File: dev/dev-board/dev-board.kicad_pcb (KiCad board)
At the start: 2 copper layers, 95 x 95 mm, 108 parts, among them J1 Conn_01x04_Pin, J2 Conn_01x14_Socket, P1 HDR-IDC-2.54-2X5P, Q1 BSS138, Q2 BSS138, Q3 BSS138, Q4 BSS138, SW1 TS342A2P, SW2 TS342A2P, SW3 TS342A2P, SW4 TS342A2P, SW6 TSC015A03526A, SW7 TSC015A03526A, SW8 TSC015A03526A, SW9 TSC015A03526A, U1 ESP32-WROVER-IE(16MB), U10 TPS2065CDBV, U11 PESD5V0U2BT, U12 PESD5V0S1BA_C5261083, U13 PCM5102APWR, U2 ESP32-S3-WROOM-1(N16R8), U3 CP2105-F01-GMR, U4 TPS2065CDBV, U5 AP7361C-33E, U6 PESD5V0U2BT, U7 PESD5V0S1BA_C5261083, U8 ZX-HY2.0-4PWZ, U9 ZX-HY2.0-4PWZ

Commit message: making CAD
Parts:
- moved R34 31.1 mm to (-100.0, 6.00), turned to 180 degrees
- moved R31 29.3 mm to (-93.3, 13.5), turned to 180 degrees
- moved R32 26.4 mm to (-93.3, 11.8), turned to 180 degrees
- moved C24 25.0 mm to (-94.5, 24.8)
- moved R30 21.4 mm to (-93.3, 15.3), turned to 180 degrees
- moved C31 18.6 mm to (-110.7, 16.2), turned to -90 degrees
- moved C22 17.8 mm to (-101.2, 19.0), turned to 90 degrees
- moved C32 15.5 mm to (-117.5, 17.8), turned to 180 degrees
- moved R29 14.9 mm to (-114.2, 17.8)
- moved C30 13.4 mm to (-105.8, 12.2), turned to 90 degrees
- moved C23 8.85 mm to (-99.5, 19.0), turned to 90 degrees
- moved LDO1 8.34 mm to (-96.5, 21.0)
- moved C29 7.86 mm to (-100.0, 8.77), turned to 180 degrees
- moved C25 7.74 mm to (-94.2, 9.00), turned to 90 degrees
- moved C28 7.71 mm to (-97.2, 8.00), turned to -90 degrees
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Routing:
- net /S3-ButtonUp: track 0.00 -> 127.9 mm, vias 0 -> 4
- net /S3-ButtonDown: track 0.00 -> 98.5 mm, vias 0 -> 6
- net /S3-ButtonCancel: track 0.00 -> 92.9 mm, vias 0 -> 6
- net /S3-ButtonEnter: track 0.00 -> 91.0 mm, vias 0 -> 8
- net +3V3: track 306.4 -> 375.0 mm, vias 13 -> 15
- net /VSPI-MOSI: track 0.00 -> 65.4 mm, vias 0 -> 3
- net /VSPI-TFT-RESET: track 0.00 -> 60.5 mm, vias 0 -> 1
- net /VSPI-SCLK: track 0.00 -> 59.2 mm, vias 0 -> 1
- net /VSPI-DC: track 0.00 -> 57.2 mm, vias 0 -> 5
- net /VSPI-CS: track 0.00 -> 55.1 mm, vias 0 -> 1
- net /VSPI-MISO: track 0.00 -> 53.6 mm, vias 0 -> 3
- net /S3-IO0: track 38.0 -> 74.1 mm, vias 2 -> 4
- net /WR-IO35: track 0.00 -> 27.3 mm
- net /WR-IO34: track 0.00 -> 25.6 mm
- net /WR-I2S-BLK: track 0.00 -> 25.0 mm
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
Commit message: making CAD
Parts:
- added REF**: MountingHole_3.2mm_M3, MountingHole:MountingHole_3.2mm_M3, F.Cu at (-120.0, 40.2)
- added REF**: MountingHole_3.2mm_M3, MountingHole:MountingHole_3.2mm_M3, F.Cu at (-120.2, -45.5)
- added REF**: MountingHole_3.2mm_M3, MountingHole:MountingHole_3.2mm_M3, F.Cu at (-34.5, 40.8)
- added REF**: MountingHole_3.2mm_M3, MountingHole:MountingHole_3.2mm_M3, F.Cu at (-34.2, -45.5)
- moved C17 5.80 mm to (-112.8, 37.8)
- moved C9 4.45 mm to (-41.0, 27.8)
- moved P1 4.12 mm to (-34.5, 30.2)
- moved LED1 2.25 mm to (-112.5, 41.0)
- moved C1 1.88 mm to (-45.2, -20.8)
- moved SW6 1.75 mm to (-120.8, -28.2)
- moved SW7 1.75 mm to (-113.0, -37.5)
- moved SW8 1.75 mm to (-120.8, -37.2)
- moved SW9 1.75 mm to (-113.0, -28.2)
- moved C2 0.96 mm to (-47.2, -18.2)
- moved U7 0.90 mm to (-42.2, -21.8), turned to 0 degrees
- moved U4 0.41 mm to (-42.2, -18.5)
- renumbered SW1 to SW1(S3-IO0), SW2 to SW2(WR-IO0), SW3 to SW3(S3-EN), SW4 to SW4(WR-EN)
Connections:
- net /CC1 renamed CC1
- net /CC2 renamed CC2
- net /D+ renamed D+
- net /D- renamed D-
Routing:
- net CC1: track 0.00 -> 32.9 mm, vias 0 -> 2
- net +3V3: track 375.0 -> 406.4 mm, vias 15 -> 17
- net VBUS: track 16.3 -> 46.9 mm, vias 0 -> 1
- net GND: track 0.00 -> 11.2 mm, vias 0 -> 498
- net D+: track 7.16 -> 16.7 mm, vias 0 -> 3
- net /S3-RMT: track 125.2 -> 115.9 mm
- net CC2: track 0.00 -> 8.19 mm
- net /S3-MTDO: track 26.0 -> 30.6 mm
- net /S3-USB-PWSW: track 84.5 -> 80.2 mm
- net /S3-MTCK: track 26.9 -> 23.7 mm
- net /S3-MTMS: track 30.3 -> 27.8 mm
- net /S3-MTDI: track 36.0 -> 33.6 mm
- net /S3-ButtonCancel: track 92.9 -> 95.0 mm, vias 6 -> 4
- net D-: track 11.7 -> 13.3 mm
- net VSYS: track 161.4 -> 159.9 mm
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- added copper zone on B.Cu, net GND
- added copper zone on F.Cu, net GND
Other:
- outline, holes or cut-outs redrawn

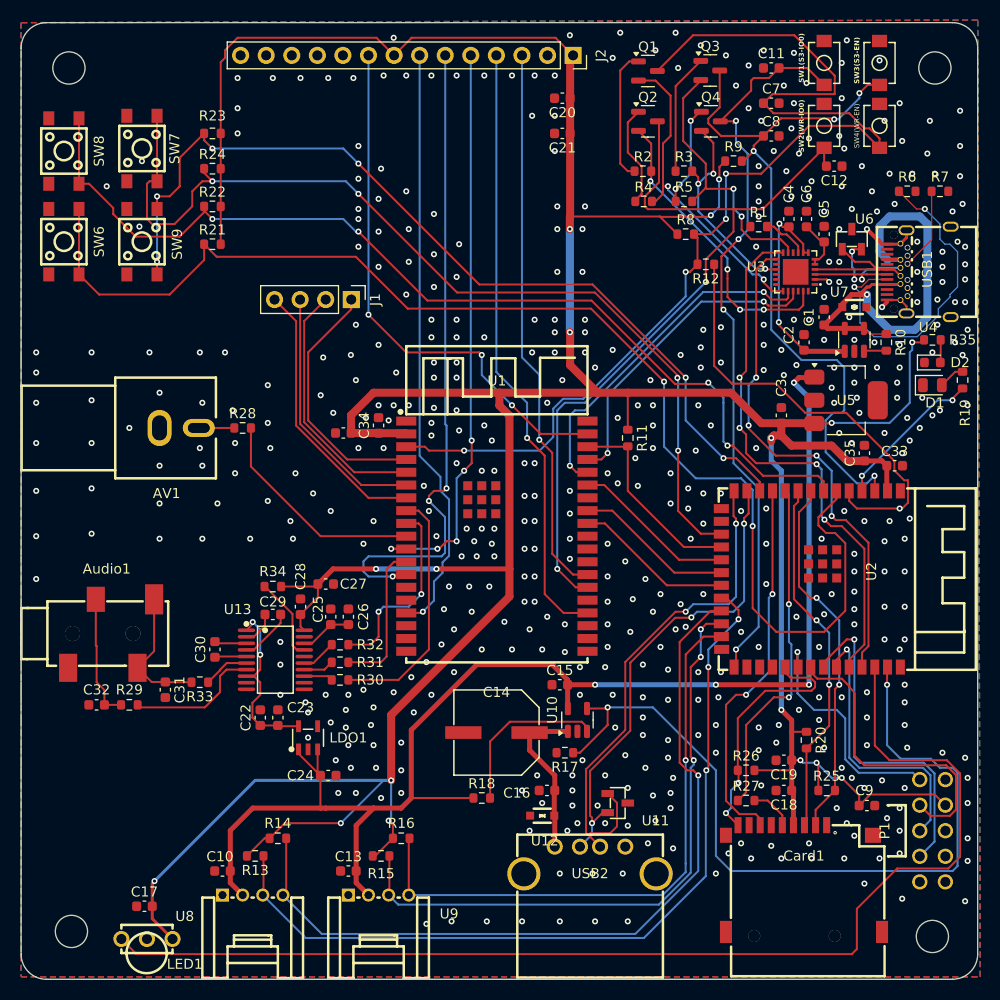
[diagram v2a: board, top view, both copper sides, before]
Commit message: finish cad. 1st step. add symbol,footprint files
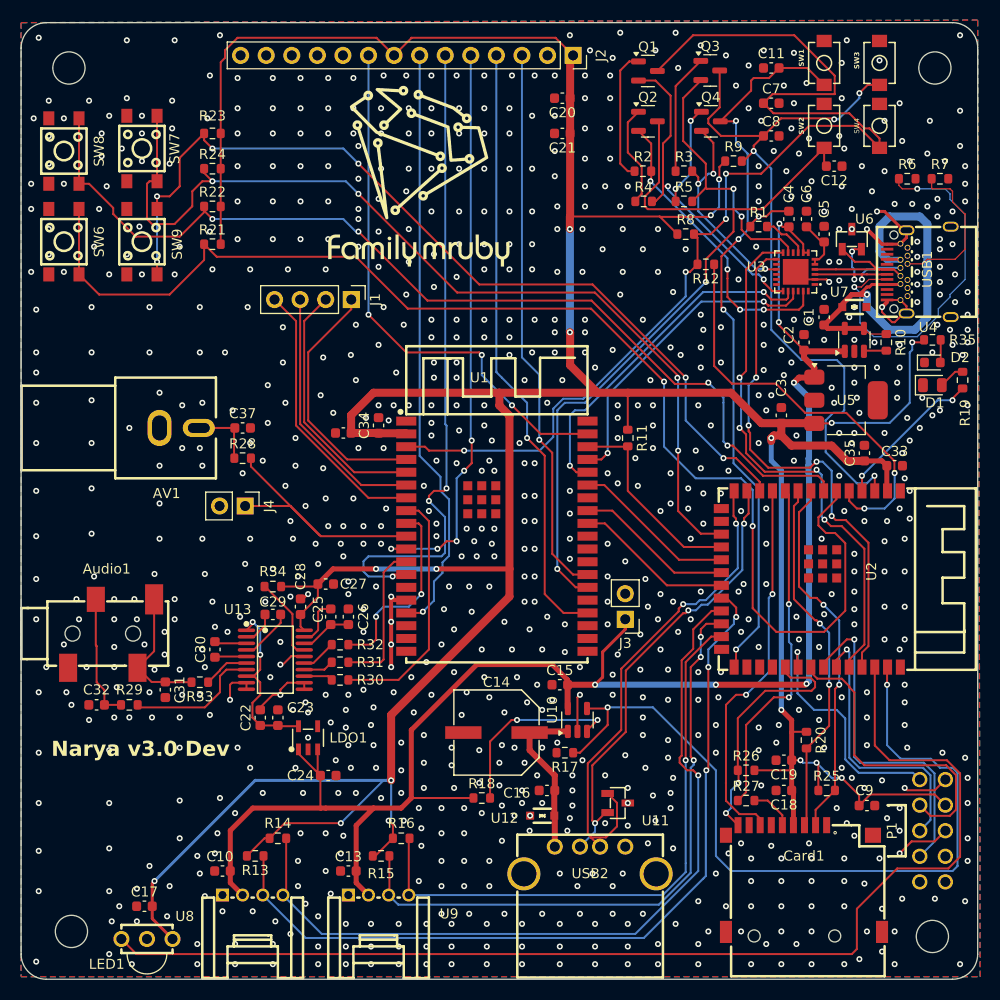
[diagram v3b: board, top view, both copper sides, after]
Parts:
- added C37: DNP, Capacitor_SMD:C_0603_1608Metric, F.Cu at (-103.0, -9.75)
- added G***: LOGO, LogoLibrary:logo_, F.Cu at (-85.5, -34.8)
- added J3: DNP Conn_01x02_Pin, Connector_PinHeader_2.54mm:PinHeader_1x02_P2.54mm_Vertical, F.Cu at (-65.0, 9.25)
- added J4: DNP Conn_01x02_Pin, Connector_PinHeader_2.54mm:PinHeader_1x02_P2.54mm_Vertical, F.Cu at (-102.8, -2.00)
- J1: value Conn_01x04_Pin -> DNP Conn_01x04_Pin
- J2: value Conn_01x14_Socket -> DNP Conn_01x14_Socket
- moved R28 3.00 mm to (-103.0, -6.75)
- moved R6 1.25 mm to (-37.0, -34.5)
- moved R7 1.25 mm to (-33.8, -34.5)
- renumbered SW1(S3-IO0) to SW1, SW2(WR-IO0) to SW2, SW3(S3-EN) to SW3, SW4(WR-EN) to SW4
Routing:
- net GND: track 11.2 -> 66.8 mm, vias 498 -> 901
- net VSYS: track 159.9 -> 170.9 mm
- net CC2: track 8.19 -> 15.8 mm
- net /WR-NTSC: track 22.1 -> 27.7 mm
- net CC1: track 32.9 -> 36.5 mm
- net Net-(AV1-Pad2): track 3.52 -> 6.57 mm
- net /S3-ResetSub: track 44.2 -> 41.6 mm, vias 1 -> 2
- net Net-(U10-~{FLT}): track 16.7 -> 19.2 mm, vias 0 -> 2
- net /S3-USB-D-: track 47.6 -> 45.8 mm
- net /S3-USB-D+: track 51.7 -> 50.0 mm
- net /TXD-ECI: track 50.4 -> 52.1 mm
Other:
- board text added: "Narya v3.0 Dev"

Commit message: complete BOM
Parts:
- removed USB1: TYPE-C 24P QCHT, easyeda2kicad:TYPE-C-SMD_TYPE-C-24P-QCHT
- added D3: LED RED, LED_SMD:LED_0603_1608Metric, F.Cu at (-79.5, 31.8)
- added R36: 1K, Resistor_SMD:R_0603_1608Metric, F.Cu at (-79.5, 30.0)
- added USBC1: TYPE-C-31-M-12, easyeda2kicad:USB-C_SMD-TYPE-C-31-M-12_1_Small, F.Cu at (-35.8, -25.2)
- C6: value 2uF -> 2.2uF
- R8, R9: value 10k -> 10K
- moved R10 0.72 mm to (-39.5, -17.7)
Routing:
- net VBUS: track 46.9 -> 31.0 mm, vias 1 -> 2
- net Net-(U10-OUT): track 16.3 -> 27.5 mm
- net GND: track 66.8 -> 56.8 mm, vias 901 -> 894
- net CC1: track 36.5 -> 32.9 mm
- net CC2: track 15.8 -> 12.8 mm, vias 0 -> 2
- net D+: track 16.7 -> 19.2 mm, vias 3 -> 4
- net D-: track 13.3 -> 15.7 mm, vias 0 -> 2
- net Net-(D3-A): track 0.00 -> 1.77 mm
- net VSYS: track 170.9 -> 172.3 mm

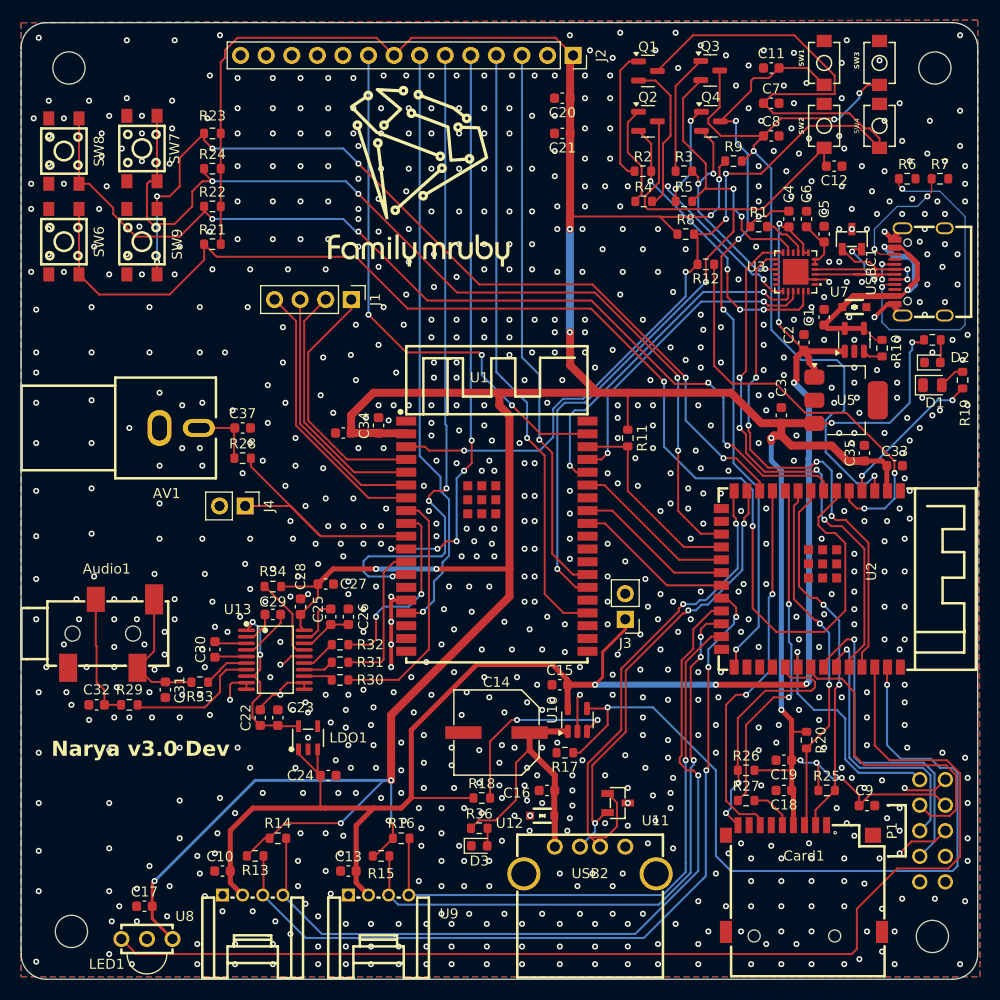
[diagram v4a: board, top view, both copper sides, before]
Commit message: change board size. change C14
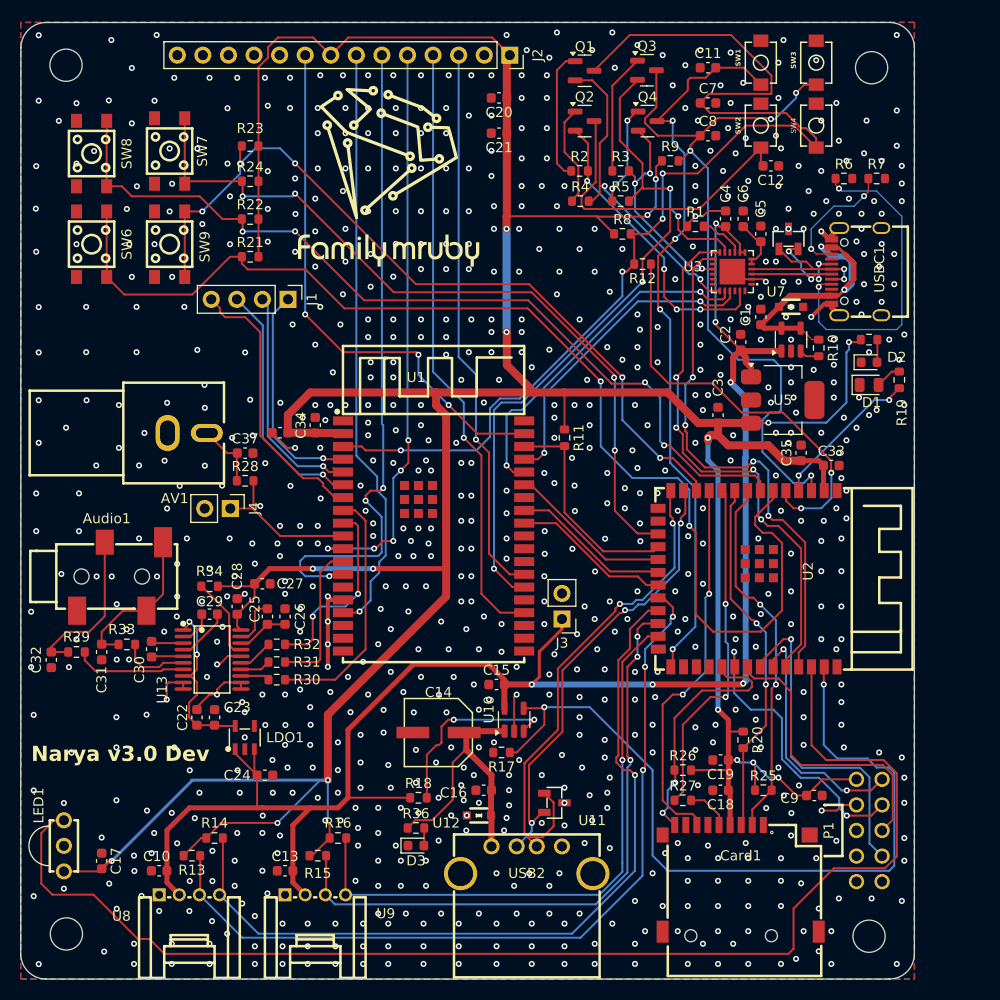
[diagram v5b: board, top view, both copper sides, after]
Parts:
- C14: footprint easyeda2kicad:CAP-SMD_BD8.0-L8.3-W8.3-RD -> easyeda2kicad:CAP-SMD_BD6.3-L6.6-W6.6-LS7.2-R-RD
- moved LED1 12.4 mm to (-120.8, 31.8), turned to -90 degrees
- moved R33 8.16 mm to (-114.5, 11.8)
- moved R29 7.42 mm to (-119.5, 12.5)
- moved C31 7.35 mm to (-117.0, 12.5)
- moved C32 6.35 mm to (-122.0, 13.3), turned to -90 degrees
- moved J1 6.29 mm to (-98.5, -22.5)
- moved R3 6.29 mm to (-65.5, -35.3)
- moved R4 6.29 mm to (-69.5, -32.3)
- moved R5 6.29 mm to (-65.5, -32.3)
- moved C1 6.29 mm to (-51.5, -20.8)
- moved C11 6.29 mm to (-56.8, -45.5)
- moved C12 6.29 mm to (-50.5, -35.8)
- moved C18 6.29 mm to (-55.5, 26.2)
- moved C19 6.29 mm to (-55.5, 23.2)
- moved C2 6.29 mm to (-53.5, -18.3)
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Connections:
- C9 pad 1: GND -> +3V3
- C9 pad 2: +3V3 -> GND
- P1 pad 1: /S3-MTCK -> +3V3
- P1 pad 2: GND -> /S3-MTMS
- P1 pad 3: /S3-MTDO -> GND
- P1 pad 4: +3V3 -> /S3-MTCK
- P1 pad 5: /S3-MTMS -> GND
- P1 pad 6: GND -> /S3-MTDO
- P1 pad 7: /S3-MTDI -> GND
- P1 pad 8: unconnected-(P1-Pad8) -> /S3-MTDI
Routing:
- net /S3-ButtonCancel: track 95.0 -> 77.0 mm
- net +3V3: track 406.4 -> 389.4 mm
- net /WR-NTSC: track 27.7 -> 15.1 mm
- net /S3-ButtonDown: track 99.9 -> 87.9 mm
- net /S3-ButtonEnter: track 91.2 -> 79.4 mm, vias 6 -> 5
- net /S3-RMT: track 115.9 -> 127.7 mm
- net /S3-ButtonUp: track 128.3 -> 117.6 mm
- net /S3-MTCK: track 23.7 -> 28.8 mm, vias 1 -> 2
- net GND: track 56.8 -> 53.2 mm, vias 894 -> 813
- net Net-(Audio1-Pad3): track 12.5 -> 16.1 mm
- net /S3-MTMS: track 27.8 -> 24.4 mm, vias 1 -> 2
- net /WR-IO36: track 25.1 -> 22.3 mm, vias 0 -> 1
- net Net-(U13-OUTR): track 13.4 -> 11.1 mm
- net Net-(Audio1-Pad2): track 13.4 -> 15.7 mm
- net Net-(U13-OUTL): track 4.62 -> 6.80 mm
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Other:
- board size 95 x 95 mm -> 88.8 x 95 mm

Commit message: fix LCSC num, improve cad
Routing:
- net VSYS: track 172.3 -> 174.9 mm, vias 6 -> 10
- net /S3-ButtonUp: track 117.6 -> 119.5 mm
- net +3V3: track 389.4 -> 391.1 mm, vias 17 -> 19
- net /WR-EN: track 113.3 -> 113.9 mm
- net /RXD-ECI: track 53.9 -> 54.5 mm
- net GND: vias 813 -> 819
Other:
- board text added: "S3-EN"
- board text added: "S3-IO"
- board text added: "WR-EN"
- board text added: "WR-IO"

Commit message: release candidadte
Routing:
- net /S3-SPI3-MISO: track 38.1 -> 39.5 mm
- net /S3-ButtonUp: track 119.5 -> 120.5 mm
- net /RXD-SCI: track 34.8 -> 35.4 mm
- net GND: vias 819 -> 798

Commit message: designing R2 board
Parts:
- removed C17: 0.1uF, Capacitor_SMD:C_0603_1608Metric
- removed G***: LOGO, LogoLibrary:logo_
- removed J1: DNP Conn_01x04_Pin, Connector_PinHeader_2.54mm:PinHeader_1x04_P2.54mm_Vertical
- removed J2: DNP Conn_01x14_Socket, Connector_PinSocket_2.54mm:PinSocket_1x14_P2.54mm_Vertical
- removed J3, J4: DNP Conn_01x02_Pin, Connector_PinHeader_2.54mm:PinHeader_1x02_P2.54mm_Vertical
- removed LED1: TSOP38238, easyeda2kicad:SENSOR-TG_TSOP38236
- removed the REF** at (-120.5, 40.5)
- removed the REF** at (-120.5, -45.8)
- removed the REF** at (-40.8, 40.7)
- removed the REF** at (-40.5, -45.5)
- removed SW9: TSC015A03526A, easyeda2kicad:SW-SMD_4P-L4.5-W4.5-P3.00-LS6.8
- added C38: 0.1uF, Capacitor_SMD:C_0603_1608Metric, F.Cu at (64.5, 203.0)
- added J5: Conn_02x10_Odd_Even, Connector_PinHeader_2.54mm:PinHeader_2x10_P2.54mm_Vertical, F.Cu at (35.1, 195.2)
- added R37: 5.1K, Resistor_SMD:R_0603_1608Metric, F.Cu at (77.8, 203.0)
- added R38: 10K, Resistor_SMD:R_0603_1608Metric, F.Cu at (86.0, 222.2)
- added REF**: MountingHole_3.2mm_M3, MountingHole:MountingHole_3.2mm_M3, F.Cu at (111.2, 256.2)
- added REF**: MountingHole_3.2mm_M3, MountingHole:MountingHole_3.2mm_M3, F.Cu at (28.8, 193.8)
- added REF**: MountingHole_3.2mm_M3, MountingHole:MountingHole_3.2mm_M3, F.Cu at (111.2, 193.8)
- added REF**: MountingHole_3.2mm_M3, MountingHole:MountingHole_3.2mm_M3, F.Cu at (28.8, 256.2)
- added RX1: TestPoint, TestPoint:TestPoint_Pad_D1.0mm, F.Cu at (92.8, 205.8)
- added RX2: TestPoint, TestPoint:TestPoint_Pad_D1.0mm, F.Cu at (82.2, 212.0)
- added SW5: TS342A2P, easyeda2kicad:KEY-SMD_L3.9-W3.0-LS5.0, F.Cu at (29.8, 203.2)
- added TP5: TestPoint, TestPoint:TestPoint_Pad_D1.0mm, F.Cu at (51.5, 222.8)
- added TX1: TestPoint, TestPoint:TestPoint_Pad_D1.0mm, F.Cu at (90.0, 205.8)
- added TX2: TestPoint, TestPoint:TestPoint_Pad_D1.0mm, F.Cu at (82.2, 208.5)
- added U14: CH340C, easyeda2kicad:SOP-16_L10.0-W3.9-P1.27-LS6.0-BL, F.Cu at (70.2, 197.1)
- added U16: PESD5V0U2BT, easyeda2kicad:SOT-23-3_L2.9-W1.3-P1.90-LS2.4-BR, F.Cu at (78.8, 200.2)
- added USBC2: TYPE-C-31-M-12, easyeda2kicad:USB-C_SMD-TYPE-C-31-M-12_1_Small, F.Cu at (82.5, 195.3)
- C4: value 1uF -> 0.1uF
- C6: value 2.2uF -> 0.1uF
- R1: value 4.7K -> 5.1K
- R19, R35, R36: value 1K -> 2K
- SW6, SW7, SW8: value TSC015A03526A -> TS342A2P; footprint easyeda2kicad:SW-SMD_4P-L4.5-W4.5-P3.00-LS6.8 -> easyeda2kicad:KEY-SMD_L3.9-W3.0-LS5.0
- U3: value CP2105-F01-GMR -> CH340C; footprint easyeda2kicad:QFN-24_L4.0-W4.0-P0.50-BL-EP2.6 -> easyeda2kicad:SOP-16_L10.0-W3.9-P1.27-LS6.0-BL
- moved Q3 295.1 mm to (86.0, 209.5)
- moved Q4 293.9 mm to (86.0, 213.2)
- moved R5 292.4 mm to (89.0, 216.0)
- moved R9 292.1 mm to (90.5, 213.8)
- moved C8 288.8 mm to (90.8, 209.5)
- moved R23 286.9 mm to (37.2, 213.0)
- moved R24 285.8 mm to (41.0, 213.0)
- moved SW8 285.7 mm to (29.8, 207.5), turned to 0 degrees
- moved R3 283.5 mm to (82.9, 206.2)
- moved SW7 282.1 mm to (37.2, 203.2), turned to 0 degrees
- moved SW6 282.1 mm to (37.2, 207.5), turned to 0 degrees
- moved R11 281.2 mm to (86.0, 224.5), turned to 0 degrees
- moved R6 280.3 mm to (104.0, 204.0), turned to 180 degrees
- moved R22 278.7 mm to (33.2, 213.0)
- moved C31 277.9 mm to (39.8, 242.0), turned to 0 degrees
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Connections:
- net CC1 renamed /CC1-1
- net CC2 renamed /CC2-1
- C4 pad 2: VSYS -> Net-(U3-V3)
- C5 pad 2: Net-(U3-VDD) -> Net-(U14-V3)
- C6 pad 2: Net-(U3-VDD) -> +3V3
- Q1 pad 2: /RTS-SCI -> /RTS2
- Q2 pad 2: /DTR-SCI -> /DTR2
- Q3 pad 2: /RTS-ECI -> /RTS1
- Q4 pad 2: /DTR-ECI -> /DTR1
- R1 pad 1: GND -> /CC1-2
- R1 pad 2: Net-(U3-~{RST}) -> GND
- R2 pad 2: /DTR-SCI -> /DTR2
- R3 pad 2: /DTR-ECI -> /DTR1
- R4 pad 2: /RTS-SCI -> /RTS2
- R5 pad 2: /RTS-ECI -> /RTS1
- SW6 pad 1: /S3-ButtonUp -> GND
- SW6 pad 2: /S3-ButtonUp -> /S3-ButtonCancel
- SW7 pad 1: /S3-ButtonCancel -> GND
- SW7 pad 2: /S3-ButtonCancel -> /S3-ButtonEnter
- SW8 pad 1: /S3-ButtonDown -> GND
- U1 pad 11: /VSPI-DC -> /WR-IO26
- U1 pad 13: /VSPI-MOSI -> /WR-IO14
- U1 pad 14: unconnected-(U1-IO12-Pad14) -> /WR-IO12
- U1 pad 16: /VSPI-SCLK -> /WR-IO13
- U1 pad 23: /VSPI-TFT-RESET -> /WR-IO15
- U1 pad 26: /VSPI-CS -> /WR-IO4
- U1 pad 29: unconnected-(U1-IO5-Pad29) -> /WR-IO5
- U1 pad 34: /RXD-SCI -> /TX2
- U1 pad 35: /TXD-SCI -> /RX2
- U1 pad 37: /VSPI-MISO -> /SPI-SYNC
- U2 pad 17: /S3-ButtonCancel -> /SPI-SYNC
- U2 pad 36: /RXD-ECI -> /TX1
- U2 pad 37: /TXD-ECI -> /RX1
- U2 pad 38: /S3-RMT -> /S3-ButtonCancel
- U3 pad 1: unconnected-(U3-~{SUSPEND}/RI_SCI-Pad1) -> GND
- U3 pad 11: /RTS-ECI -> unconnected-(U3-~{RI}-Pad11)
- U3 pad 12: /RXD-ECI -> unconnected-(U3-~{DCD}-Pad12)
- U3 pad 13: /TXD-ECI -> /DTR1
- U3 pad 14: unconnected-(U3-GPIO.1_ECI/DSR_ECI-Pad14) -> /RTS1
- U3 pad 15: /DTR-ECI -> unconnected-(U3-R232-Pad15)
- U3 pad 16: unconnected-(U3-NC/DCD_ECI/VPP-Pad16) -> +3V3
- U3 pad 2: GND -> /TX1
- U3 pad 3: D+ -> /RX1
- U3 pad 4: D- -> Net-(U3-V3)
- U3 pad 5: Net-(U3-VDD) -> /D+1
- U3 pad 6: Net-(U3-VDD) -> /D-1
- U3 pad 7: VSYS -> unconnected-(U3-NC.-Pad7)
- U3 pad 8: VSYS -> unconnected-(U3-~{OUT}-Pad8)
- U3 pad 9: Net-(U3-~{RST}) -> unconnected-(U3-~{CTS}-Pad9)
- U6 pad 1: D- -> /D-1
- U6 pad 2: D+ -> /D+1
- USBC1 pad A6: D+ -> /D+1
- USBC1 pad A7: D- -> /D-1
- USBC1 pad B6: D+ -> /D+1
- USBC1 pad B7: D- -> /D-1
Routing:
- net +3V3: track 391.1 -> 37.0 mm, vias 19 -> 12
- net VSYS: track 174.9 -> 37.1 mm, vias 10 -> 13
- net /S3-RMT: track 127.7 -> 0.00 mm
- net /S3-ButtonUp: track 120.5 -> 0.00 mm, vias 2 -> 0
- net /WR-EN: track 113.9 -> 0.00 mm, vias 4 -> 0
- net /S3-ButtonDown: track 87.9 -> 0.00 mm, vias 4 -> 0
- net /S3-I2C1-SDA: track 82.0 -> 0.00 mm, vias 3 -> 0
- net /S3-I2C1-SCL: track 80.4 -> 0.00 mm, vias 1 -> 0
- net /S3-ButtonEnter: track 79.4 -> 0.00 mm, vias 5 -> 0
- net /WR-IO0: track 79.3 -> 0.00 mm, vias 2 -> 0
- net /S3-ButtonCancel: track 77.0 -> 0.00 mm, vias 4 -> 0
- net /S3-EN: track 74.1 -> 0.00 mm, vias 4 -> 0
- net /S3-IO0: track 74.1 -> 0.00 mm, vias 4 -> 0
- net /S3-USB-PWSW: track 80.2 -> 12.5 mm, vias 2 -> 0
- net /VSPI-MOSI: track 65.4 -> 0.00 mm, vias 3 -> 0
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- added copper zone on In2.Cu, net +3V3
- added copper zone on In1.Cu, net GND
- added copper zone on In2.Cu, net VSYS
- removed copper zone on B.Cu, net GND
- removed copper zone on F.Cu, net GND
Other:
- board size 88.8 x 95 mm -> 90 x 70 mm
- copper layers 2 -> 4
- board text removed: "Narya v3.0 Dev"
- board text removed: "S3-EN"
- board text removed: "S3-IO"
- board text removed: "WR-EN"
- board text removed: "WR-IO"
